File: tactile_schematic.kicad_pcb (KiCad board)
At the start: 2 copper layers, 109.6 x 67.4 mm, 37 parts, among them IC1 CY8C4145PVI-PS431, J1 Conn_01x02, J2 Conn_01x04, J3 Conn_01x04, J4 Conn_01x02

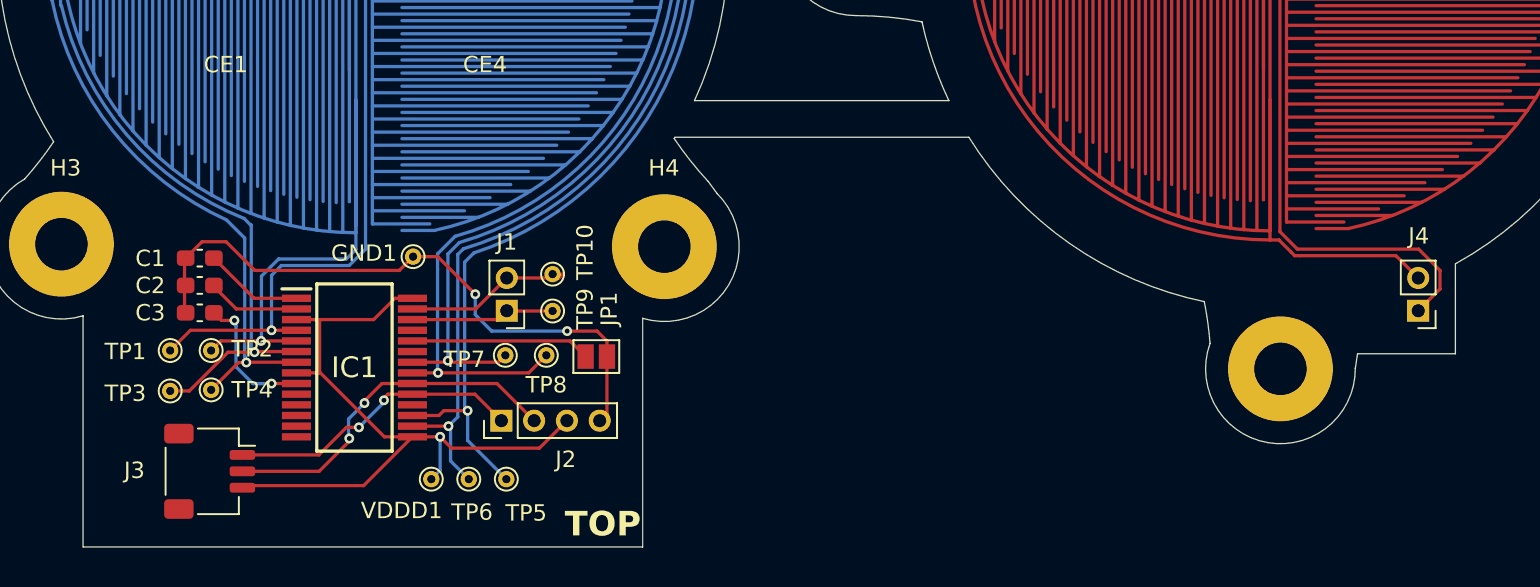
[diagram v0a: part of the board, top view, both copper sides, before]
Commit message: redid layout, pushed circuits down a bit
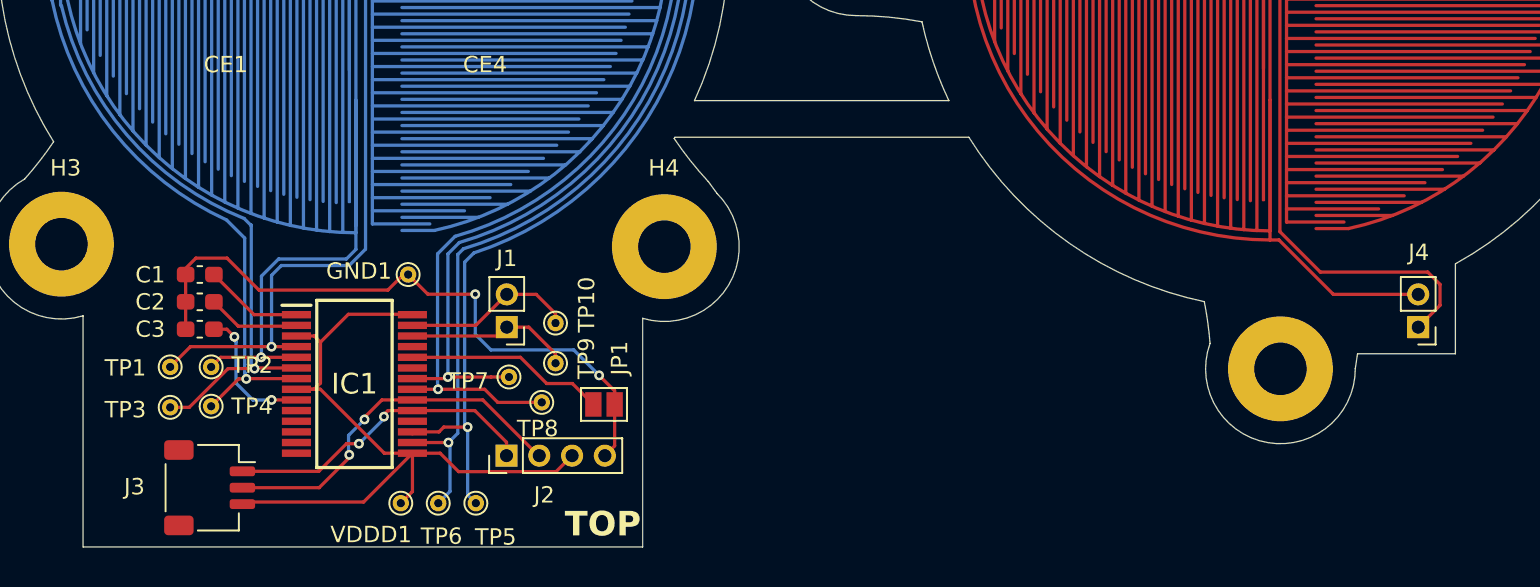
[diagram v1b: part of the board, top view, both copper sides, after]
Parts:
- moved TP9 3.19 mm to (198.5, 76.9)
- moved TP10 2.99 mm to (198.5, 74.4)
- moved JP1 2.96 mm to (201.4, 79.4)
- moved TP8 2.89 mm to (197.7, 79.2)
- moved TP5 2.37 mm to (193.6, 85.4)
- moved TP6 2.37 mm to (191.3, 85.4)
- moved VDDD1 2.37 mm to (189.1, 85.4)
- moved J2 2.16 mm to (195.5, 82.5)
- moved TP7 1.34 mm to (195.7, 77.7)
- moved GND1 1.13 mm to (189.5, 71.5)
- moved C1 1.00 mm to (176.8, 71.5)
- moved C2 1.00 mm to (176.8, 73.1)
- moved C3 1.00 mm to (176.8, 74.8)
- moved IC1 1.00 mm to (186.2, 78.1)
- moved J1 1.00 mm to (195.5, 74.7)
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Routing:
- net P5.2: track 82.5 -> 84.4 mm
- net VDDA_1: track 44.8 -> 46.5 mm, vias 1 -> 0
- net P5.3: track 64.9 -> 66.4 mm
- net P3.1: track 27.6 -> 29.1 mm
- net Net-(IC1-XRES): track 11.0 -> 12.2 mm
- net P3.6: track 18.2 -> 19.5 mm
- net P0.1: track 38.6 -> 39.8 mm
- net P1.3: track 36.0 -> 37.0 mm
- net P1.2: track 45.4 -> 46.4 mm
- net P1.1: track 32.6 -> 33.6 mm
- net P1.0: track 42.9 -> 43.9 mm
- net GND: track 38.7 -> 39.6 mm
- net P3.7: track 21.9 -> 22.7 mm
- net P3.2: track 45.5 -> 46.2 mm

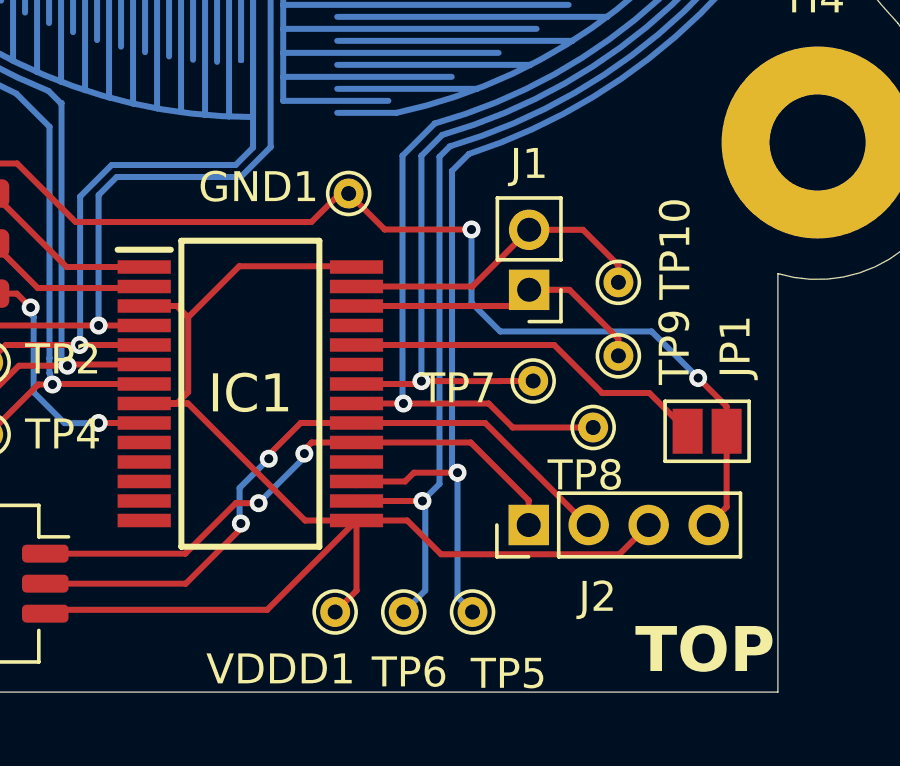
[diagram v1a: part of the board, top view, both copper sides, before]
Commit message: fixed silkscreen
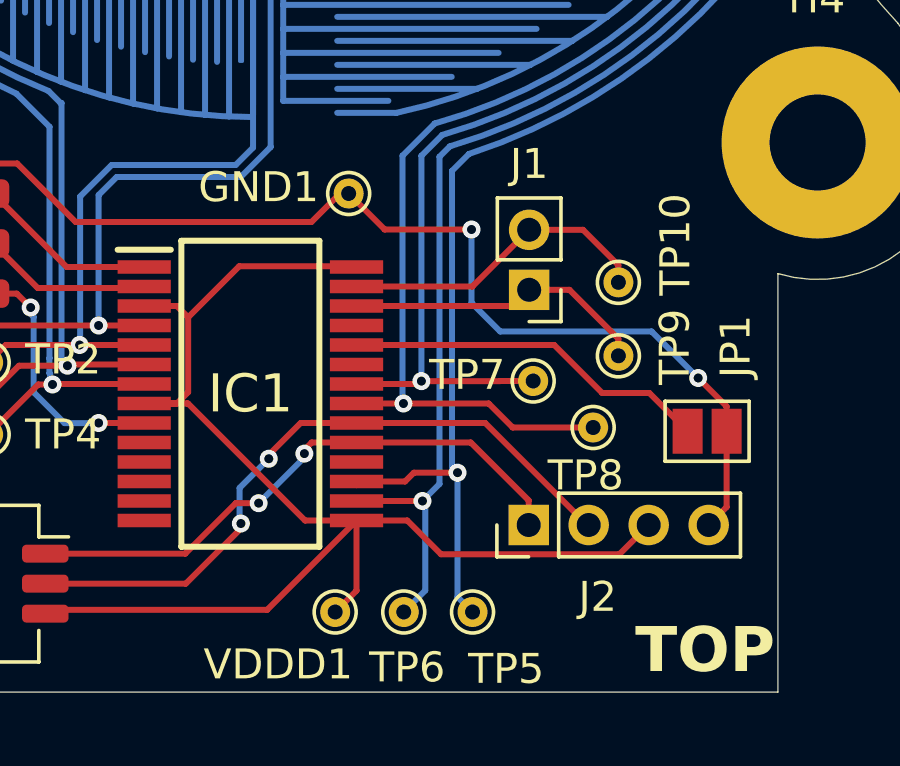
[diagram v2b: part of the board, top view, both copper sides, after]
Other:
- board text removed: "H2"
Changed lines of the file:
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@@
 		(tags "test point THT pad")
 		(property "Reference" "TP5"
-			(at -2.066001 1.2093 0)
+			(at -1.9 1.120555 0)
 			(layer "F.SilkS")
 			(effects
@@
 		(tags "test point THT pad")
 		(property "Reference" "TP6"
-			(at 0.202745 2.016001 180)
+			(at 0.114 1.85 180)
 			(layer "F.SilkS")
 			(effects
@@
 		(tags "test point THT pad")
 		(property "Reference" "TP10"
-			(at -1.9 1.124 270)
+			(at -1.9 1.26154 270)
 			(layer "F.SilkS")
 			(effects
@@
 		(tags "test point THT pad")
 		(property "Reference" "TP7"
-			(at 2.5 -0.25 180)
+			(at 2.2 0.2 180)
 			(layer "F.SilkS")
 			(effects
@@
 		(tags "test point THT pad")
 		(property "Reference" "VDDD1"
-			(at 1.811255 -1.916001 180)
+			(at 1.9 -1.75 180)
 			(layer "F.SilkS")
 			(effects
@@
 		)
 	)
-	(gr_text "H2"
-		(at 186.987098 54.7 0)
-		(layer "B.SilkS")
-		(effects
-			(font
-				(size 1 1)
-				(thickness 0.15)
-			)
-			(justify mirror)
-		)
-	)

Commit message: many changes
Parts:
- added C4: 0.1uF, Capacitor_SMD:C_0603_1608Metric_Pad1.08x0.95mm_HandSolder, F.Cu at (175.8, 79.2)
- added C5: 1uF, Capacitor_SMD:C_0603_1608Metric_Pad1.08x0.95mm_HandSolder, F.Cu at (190.5, 86.2)
- added C7: 470n, Capacitor_SMD:C_0603_1608Metric_Pad1.08x0.95mm_HandSolder, F.Cu at (189.7, 71.6)
- added C8: 470n, Capacitor_SMD:C_0603_1608Metric_Pad1.08x0.95mm_HandSolder, F.Cu at (192.4, 76.3)
- added J5: Conn_ARM_SWD_TagConnect_TC2030-NL, Connector:Tag-Connect_TC2030-IDC-NL_2x03_P1.27mm_Vertical, F.Cu at (183.5, 86.0)
- added R1: 330, Resistor_SMD:R_0603_1608Metric_Pad0.98x0.95mm_HandSolder, F.Cu at (195.2, 82.7)
- added R10: 560, Resistor_SMD:R_0603_1608Metric_Pad0.98x0.95mm_HandSolder, B.Cu at (194.2, 78.4)
- added R11: 560, Resistor_SMD:R_0603_1608Metric_Pad0.98x0.95mm_HandSolder, B.Cu at (176.4, 82.8)
- added R12: 560, Resistor_SMD:R_0603_1608Metric_Pad0.98x0.95mm_HandSolder, B.Cu at (176.4, 81.2)
- added R13: 560, Resistor_SMD:R_0603_1608Metric_Pad0.98x0.95mm_HandSolder, F.Cu at (200.1, 74.8)
- added R14: 560, Resistor_SMD:R_0603_1608Metric_Pad0.98x0.95mm_HandSolder, F.Cu at (200.0, 72.8)
- added R2: 330, Resistor_SMD:R_0603_1608Metric_Pad0.98x0.95mm_HandSolder, F.Cu at (193.7, 82.7)
- added R3: 330, Resistor_SMD:R_0603_1608Metric_Pad0.98x0.95mm_HandSolder, F.Cu at (176.2, 85.2)
- added R4: 330, Resistor_SMD:R_0603_1608Metric_Pad0.98x0.95mm_HandSolder, F.Cu at (178.6, 86.1)
- added R5: 560, Resistor_SMD:R_0603_1608Metric_Pad0.98x0.95mm_HandSolder, B.Cu at (178.5, 74.4)
- added R6: 560, Resistor_SMD:R_0603_1608Metric_Pad0.98x0.95mm_HandSolder, B.Cu at (176.9, 74.0)
- added R7: 560, Resistor_SMD:R_0603_1608Metric_Pad0.98x0.95mm_HandSolder, B.Cu at (175.3, 74.0)
- added R8: 560, Resistor_SMD:R_0603_1608Metric_Pad0.98x0.95mm_HandSolder, B.Cu at (173.7, 74.0)
- added R9: 560, Resistor_SMD:R_0603_1608Metric_Pad0.98x0.95mm_HandSolder, B.Cu at (195.9, 78.4)
- added TP11: TestPoint, TestPoint:TestPoint_THTPad_D1.0mm_Drill0.5mm, F.Cu at (174.6, 87.0)
- added TP12: TestPoint, TestPoint:TestPoint_THTPad_D1.0mm_Drill0.5mm, F.Cu at (176.6, 87.1)
- C3: value 0.1uF -> 2.2n
- J2: footprint Connector_PinHeader_2.00mm:PinHeader_1x04_P2.00mm_Vertical -> Connector_PinHeader_1.27mm:PinHeader_1x04_P1.27mm_Vertical
- J3: footprint Connector_JST:JST_SH_SM03B-SRSS-TB_1x03-1MP_P1.00mm_Horizontal -> Connector_JST:JST_SH_SM04B-SRSS-TB_1x04-1MP_P1.00mm_Horizontal
- moved TP8 24.0 mm to (173.7, 81.0)
- moved J3 22.8 mm to (200.1, 85.0), turned to 0 degrees
- moved TP7 22.6 mm to (173.7, 83.1)
- moved GND1 19.3 mm to (171.0, 77.0), turned to -90 degrees
- moved C3 15.7 mm to (192.4, 72.9), turned to 90 degrees
- moved JP1 14.7 mm to (188.4, 86.2), turned to 90 degrees
- moved VDDD1 6.07 mm to (195.1, 85.9)
- moved TP4 4.72 mm to (173.3, 77.3)
- moved TP1 4.33 mm to (179.0, 78.7)
- moved C1 4.17 mm to (178.8, 75.1)
- moved TP10 4.09 mm to (200.4, 70.8)
- moved J2 4.08 mm to (198.8, 80.1)
- moved TP9 3.51 mm to (202.0, 77.0)
- moved TP6 2.86 mm to (191.9, 82.6)
- moved TP3 2.29 mm to (175.4, 77.3)
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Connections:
- C1 pad 1: Net-(IC1-VCCD) -> VDD
- C2 pad 1: Net-(IC1-VSSD) -> Net-(IC1-VCCD)
- C3 pad 1: Net-(IC1-VSSA) -> Net-(IC1-P5.2)
- CE1 pad 1: P1.0 -> Net-(CE1-Pad1)
- CE1 pad 2: P1.1 -> Net-(CE1-Pad2)
- CE2 pad 1: P1.2 -> Net-(CE2-Pad1)
- CE2 pad 2: P1.3 -> Net-(CE2-Pad2)
- CE3 pad 1: P3.2 -> Net-(CE3-Pad1)
- CE3 pad 2: P3.1 -> Net-(CE3-Pad2)
- CE4 pad 1: P0.1 -> Net-(CE4-Pad1)
- CE4 pad 2: P0.0 -> Net-(CE4-Pad2)
- CE5 pad 1: P5.2 -> Net-(J1-Pin_1)
- CE5 pad 2: P5.3 -> Net-(J1-Pin_2)
- CE6 pad 1: P5.2 -> Net-(J1-Pin_1)
- CE6 pad 2: P5.3 -> Net-(J1-Pin_2)
- CE7 pad 1: P5.2 -> Net-(J1-Pin_1)
- CE7 pad 2: P5.3 -> Net-(J1-Pin_2)
- CE8 pad 1: P5.2 -> Net-(J1-Pin_1)
- CE8 pad 2: P5.3 -> Net-(J1-Pin_2)
- IC1 pad 10: unconnected-(IC1-P2.0-Pad10) -> Net-(IC1-P2.0)
- IC1 pad 11: unconnected-(IC1-P2.1-Pad11) -> Net-(IC1-P2.1)
- IC1 pad 12: unconnected-(IC1-P2.2-Pad12) -> CAP4B
- IC1 pad 13: unconnected-(IC1-P2.3-Pad13) -> CAP4A
- IC1 pad 15: VDDA_1 -> VDD
- IC1 pad 16: P3.1 -> CAP3A
- IC1 pad 17: P3.2 -> CAP3B
- IC1 pad 18: unconnected-(IC1-P3.3-Pad18) -> CAP0A
- IC1 pad 19: P3.6 -> Net-(IC1-P3.6)
- IC1 pad 2: Net-(IC1-VSSD) -> GND
- IC1 pad 20: P3.7 -> Net-(IC1-P3.7)
- IC1 pad 21: P0.0 -> Net-(IC1-P0.0)
- IC1 pad 22: P0.1 -> Net-(IC1-P0.1)
- IC1 pad 23: unconnected-(IC1-P0.2-Pad23) -> CAP0B
- IC1 pad 24: Net-(IC1-XRES) -> /RESET
- IC1 pad 25: unconnected-(IC1-P5.0-Pad25) -> Net-(IC1-P5.0)
- IC1 pad 26: P5.2 -> Net-(IC1-P5.2)
- IC1 pad 27: P5.3 -> Net-(IC1-P5.3)
- IC1 pad 28: VDDA_1 -> VDD
- IC1 pad 3: VDDA_1 -> VDD
- IC1 pad 4: P1.0 -> CAP2B
- IC1 pad 5: P1.1 -> CAP2A
- IC1 pad 6: P1.2 -> CAP1B
- IC1 pad 7: P1.3 -> CAP1A
- IC1 pad 8: VDDA_1 -> VDD
- IC1 pad 9: Net-(IC1-VSSA) -> GND
- J1 pad 1: P5.2 -> Net-(J1-Pin_1)
- J1 pad 2: P5.3 -> Net-(J1-Pin_2)
- J2 pad 1: P3.6 -> GND
- J2 pad 2: P3.7 -> VDD
- J2 pad 3: VDDA_1 -> SDA
- J2 pad 4: GND -> SCL
- J3 pad 1: P3.6 -> GND
- J3 pad 2: P3.7 -> VDD
- J3 pad 3: VDDA_1 -> SDA
- J4 pad 1: P5.2 -> Net-(J1-Pin_1)
- J4 pad 2: P5.3 -> Net-(J1-Pin_2)
- JP1 pad 1: Net-(IC1-XRES) -> GND
- JP1 pad 2: GND -> /RESET
- TP1 pad 1: P1.0 -> CAP1A
- TP10 pad 1: P5.3 -> CAP0B
- TP2 pad 1: P1.1 -> CAP1B
- TP3 pad 1: P1.2 -> CAP2A
- TP4 pad 1: P1.3 -> CAP2B
- TP5 pad 1: P3.2 -> CAP3A
- TP6 pad 1: P3.1 -> CAP3B
- TP7 pad 1: P0.1 -> CAP4A
- TP8 pad 1: P0.0 -> CAP4B
- TP9 pad 1: P5.2 -> CAP0A
- VDDD1 pad 1: VDDA_1 -> VDD
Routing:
- net P5.2: track 84.4 -> 0.00 mm
- net Net-(J1-Pin_1): track 0.00 -> 77.9 mm
- net P5.3: track 66.4 -> 0.00 mm
- net Net-(J1-Pin_2): track 0.00 -> 59.5 mm
- net Net-(CE4-Pad1): track 0.00 -> 48.1 mm
- net VDDA_1: track 46.5 -> 0.00 mm
- net P1.2: track 46.4 -> 0.00 mm, vias 1 -> 0
- net P3.2: track 46.2 -> 0.00 mm, vias 1 -> 0
- net P1.0: track 43.9 -> 0.00 mm, vias 1 -> 0
- net P0.1: track 39.8 -> 0.00 mm, vias 1 -> 0
- net P1.3: track 37.0 -> 0.00 mm, vias 1 -> 0
- net Net-(CE2-Pad1): track 0.00 -> 35.8 mm
- net Net-(CE3-Pad1): track 0.00 -> 35.2 mm
- net Net-(CE1-Pad1): track 0.00 -> 34.6 mm
- net P1.1: track 33.6 -> 0.00 mm, vias 1 -> 0
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- added copper zone on B.Cu, net GND
- added copper zone on F.Cu, net GND
- added copper zone on B.Cu, net VDD

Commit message: ok
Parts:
- added REF**: COIL_GENERATOR, COIL_GENERATOR, F.Cu at (133.0, 43.0)
- CE1, CE2, CE3, CE4: footprint PCB Coils:COIL_GENERATOR_1 -> ECE382N:COIL_GENERATOR; moved to B.Cu
- CE5, CE6, CE7, CE8: footprint PCB Coils:COIL_GENERATOR -> ECE382N:COIL_GENERATOR
- moved CE4 1.08 mm to (187.3, 50.1)
- moved CE2 1.06 mm to (186.6, 51.2)
- moved CE1 0.56 mm to (186.3, 50.3), turned to 90 degrees
- moved CE3 0.56 mm to (187.6, 50.9), turned to -90 degrees
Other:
- board text added: "up to 100 fins 36mm OD 0.4 spacing 0.4 thickness 2.5 gap"
